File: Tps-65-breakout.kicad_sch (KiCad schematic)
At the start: 6 parts, among them J1 Conn_01x06_Pin, J2 Conn_01x06_Socket

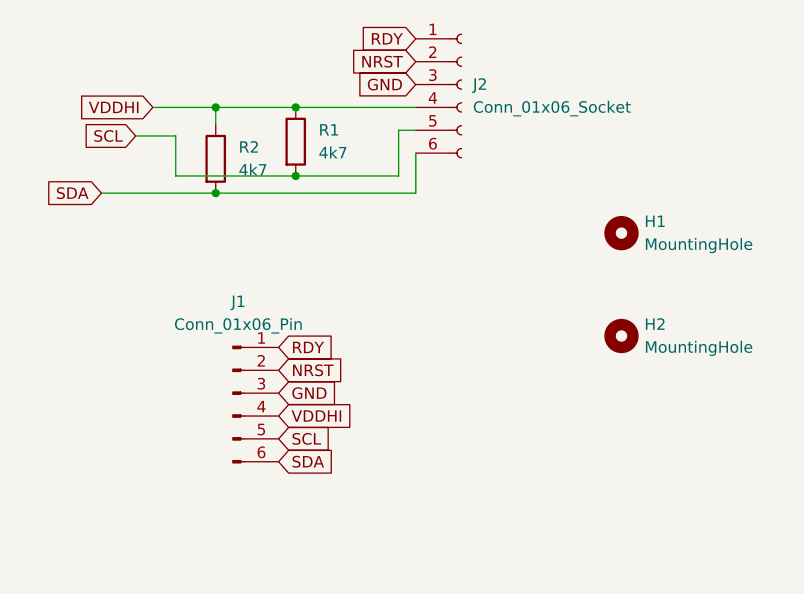
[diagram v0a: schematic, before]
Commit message: improved routing and grounded mounting holes
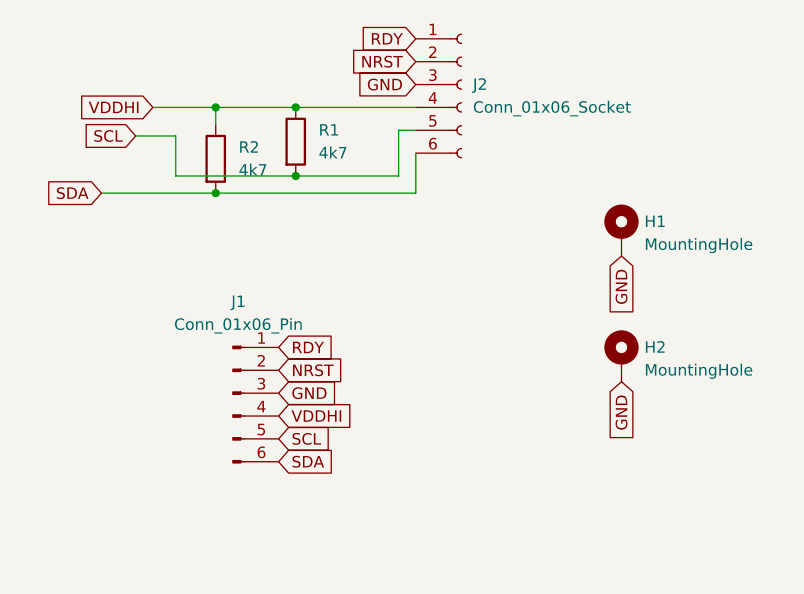
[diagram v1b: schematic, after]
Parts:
- H1, H2: footprint MountingHole:MountingHole_2.2mm_M2 -> MountingHole:MountingHole_2.2mm_M2_Pad; symbol Mechanical:MountingHole -> Mechanical:MountingHole_Pad
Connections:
- net GND: now also H1.1, H2.1
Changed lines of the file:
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@@
+    )
+  )
+  (global_label "GND" (shape input) (at 222.25 90.17 270) (fields_autoplaced)
+    (effects (font (size 1.27 1.27)) (justify right))
+    (property "Intersheetrefs" "${INTERSHEET_REFS}" (at 222.25 96.9463 90)
+      (effects (font (size 1.27 1.27)) (justify right) hide)
     )
   )
@@
     (effects (font (size 1.27 1.27)) (justify right))
     (property "Intersheetrefs" "${INTERSHEET_REFS}" (at 161.7103 59.69 0)
+      (effects (font (size 1.27 1.27)) (justify right) hide)
+    )
+  )
+  (global_label "GND" (shape input) (at 222.25 76.2 270) (fields_autoplaced)
+    (effects (font (size 1.27 1.27)) (justify right))
+    (property "Intersheetrefs" "${INTERSHEET_REFS}" (at 222.25 82.9763 90)
       (effects (font (size 1.27 1.27)) (justify right) hide)
     )
@@
     (pin "6")
     (instances
-      (project "Tps-xx-breakout"
+      (project "Tps-65-breakout"
         (path "/2cbe04c3-122d-4cbd-b6ed-decb93773a4a"
           (reference "J1") (unit 1)
@@
     )
   )
-  (symbol (lib_id "Mechanical:MountingHole") (at 222.25 85.09 0) (unit 1)
+  (symbol (lib_id "Mechanical:MountingHole_Pad") (at 222.25 87.63 0) (unit 1)
     (in_bom yes) (on_board yes) (dnp no) (fields_autoplaced)
-    (property "Reference" "H2" (at 224.79 83.82 0)
+    (property "Reference" "H2" (at 224.79 86.36 0)
       (effects (font (size 1.27 1.27)) (justify left))
     )
-    (property "Value" "MountingHole" (at 224.79 86.36 0)
+    (property "Value" "MountingHole" (at 224.79 88.9 0)
       (effects (font (size 1.27 1.27)) (justify left))
     )
-    (property "Footprint" "MountingHole:MountingHole_2.2mm_M2" (at 222.25 85.09 0)
+    (property "Footprint" "MountingHole:MountingHole_2.2mm_M2_Pad" (at 222.25 87.63 0)
       (effects (font (size 1.27 1.27)) hide)
     )
-    (property "Datasheet" "~" (at 222.25 85.09 0)
+    (property "Datasheet" "~" (at 222.25 87.63 0)
       (effects (font (size 1.27 1.27)) hide)
     )
+    (pin "1")
     (instances
-      (project "Tps-xx-breakout"
+      (project "Tps-65-breakout"
         (path "/2cbe04c3-122d-4cbd-b6ed-decb93773a4a"
           (reference "H2") (unit 1)
@@
     (pin "6")
     (instances
-      (project "Tps-xx-breakout"
+      (project "Tps-65-breakout"
         (path "/2cbe04c3-122d-4cbd-b6ed-decb93773a4a"
           (reference "J2") (unit 1)
@@
     )
   )
-  (symbol (lib_id "Mechanical:MountingHole") (at 222.25 73.66 0) (unit 1)
+  (symbol (lib_id "Mechanical:MountingHole_Pad") (at 222.25 73.66 0) (unit 1)
     (in_bom yes) (on_board yes) (dnp no) (fields_autoplaced)
     (property "Reference" "H1" (at 224.79 72.39 0)
@@
       (effects (font (size 1.27 1.27)) (justify left))
     )
-    (property "Footprint" "MountingHole:MountingHole_2.2mm_M2" (at 222.25 73.66 0)
+    (property "Footprint" "MountingHole:MountingHole_2.2mm_M2_Pad" (at 222.25 73.66 0)
       (effects (font (size 1.27 1.27)) hide)
     )
@@
       (effects (font (size 1.27 1.27)) hide)
     )
+    (pin "1")
     (instances
-      (project "Tps-xx-breakout"
+      (project "Tps-65-breakout"
         (path "/2cbe04c3-122d-4cbd-b6ed-decb93773a4a"
           (reference "H1") (unit 1)
@@
     (pin "2")
     (instances
-      (project "Tps-xx-breakout"
+      (project "Tps-65-breakout"
         (path "/2cbe04c3-122d-4cbd-b6ed-decb93773a4a"
           (reference "R2") (unit 1)
@@
     (pin "2")
     (instances
-      (project "Tps-xx-breakout"
+      (project "Tps-65-breakout"
         (path "/2cbe04c3-122d-4cbd-b6ed-decb93773a4a"
           (reference "R1") (unit 1)

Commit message: reversed pin order, grounded ffc connector, added silkscreens
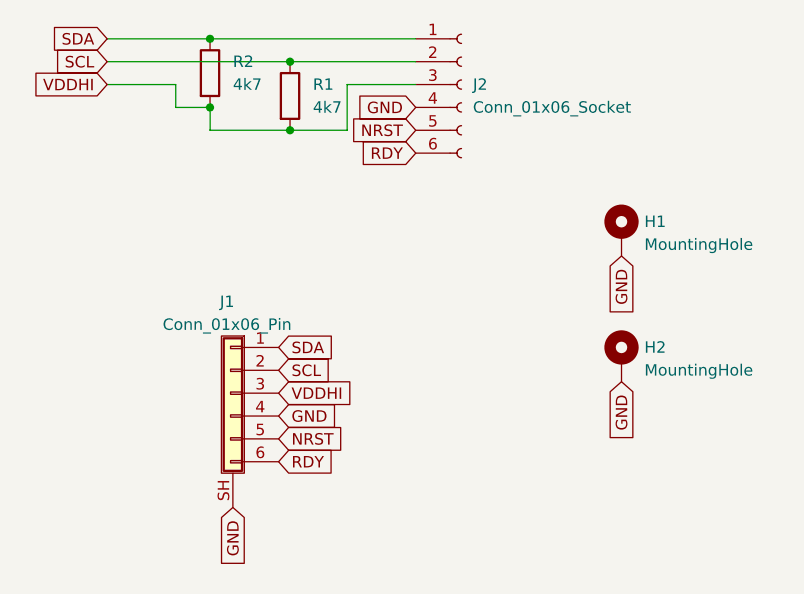
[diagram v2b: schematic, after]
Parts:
- J1: symbol Connector:Conn_01x06_Pin -> Connector_Generic_Shielded:Conn_01x06_Shielded
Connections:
- net GND: now also J1.4 (Pin_4), J1.SH (Shield), J2.4 (Pin_4); no longer J1.3 (Pin_3), J2.3 (Pin_3)
- net NRST: now also J1.5 (Pin_5), J2.5 (Pin_5); no longer J1.2 (Pin_2), J2.2 (Pin_2)
- net RDY: now also J1.6 (Pin_6), J2.6 (Pin_6); no longer J1.1 (Pin_1), J2.1 (Pin_1)
- net SCL: now also J1.2 (Pin_2), J2.2 (Pin_2), R1.1; no longer J1.5 (Pin_5), J2.5 (Pin_5), R1.2
- net SDA: now also J1.1 (Pin_1), J2.1 (Pin_1), R2.1; no longer J1.6 (Pin_6), J2.6 (Pin_6), R2.2
- net VDDHI: now also J1.3 (Pin_3), J2.3 (Pin_3), R1.2, R2.2; no longer J1.4 (Pin_4), J2.4 (Pin_4), R1.1, R2.1
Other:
- moved on the sheet: R1, R2
